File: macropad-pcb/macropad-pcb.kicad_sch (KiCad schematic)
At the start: 34 parts, among them SW1 SW_Push, U1 ATmega32U4-A, Y1 16MHz

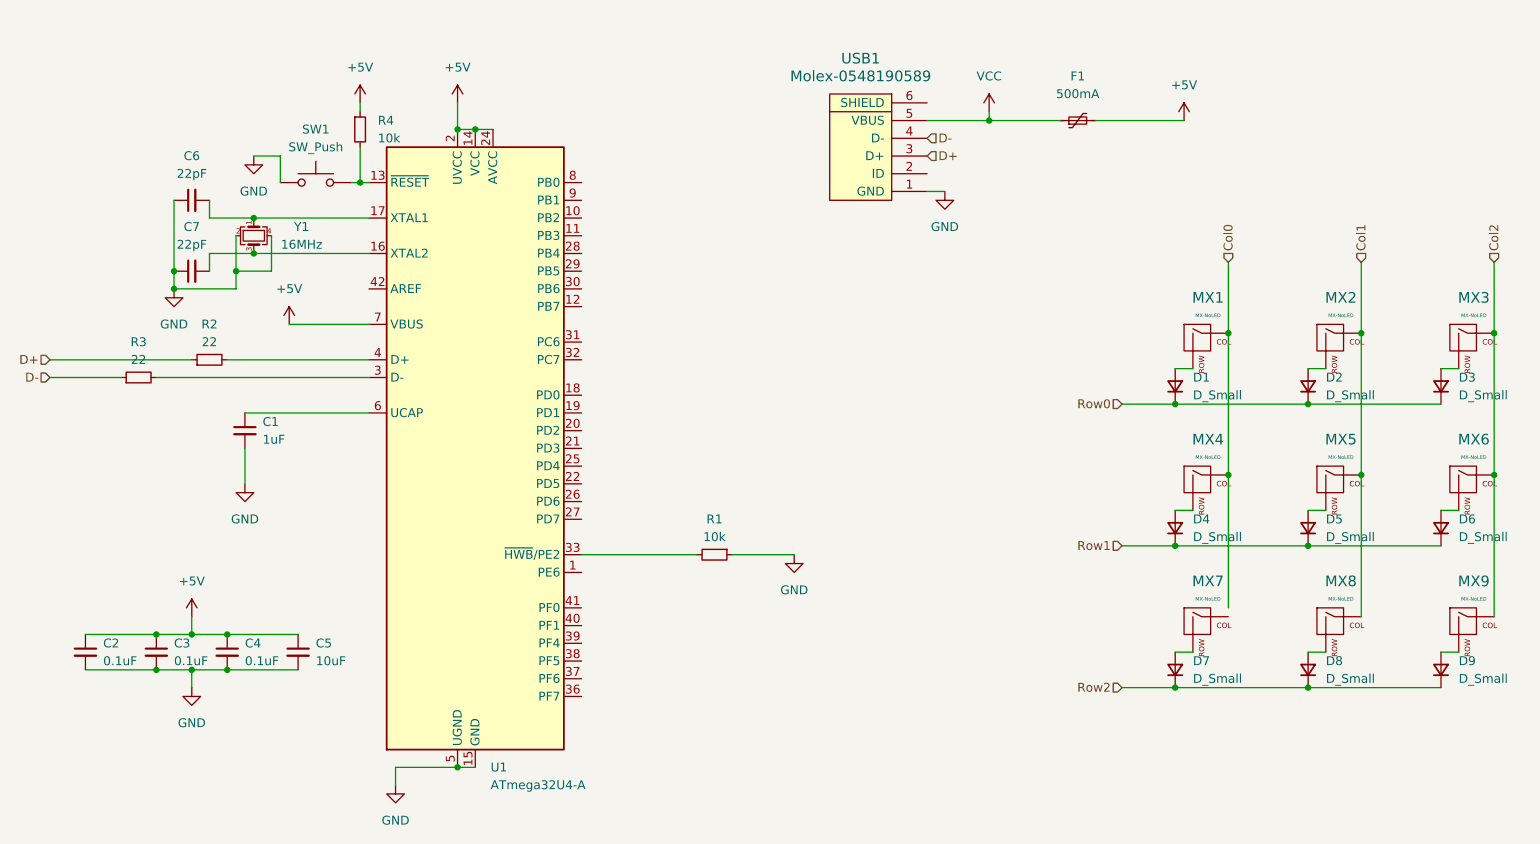
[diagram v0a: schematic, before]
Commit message: removed libraries in favor of using libraries straight from kicad, removed tracking of backups folder in version control, created and routed pcb
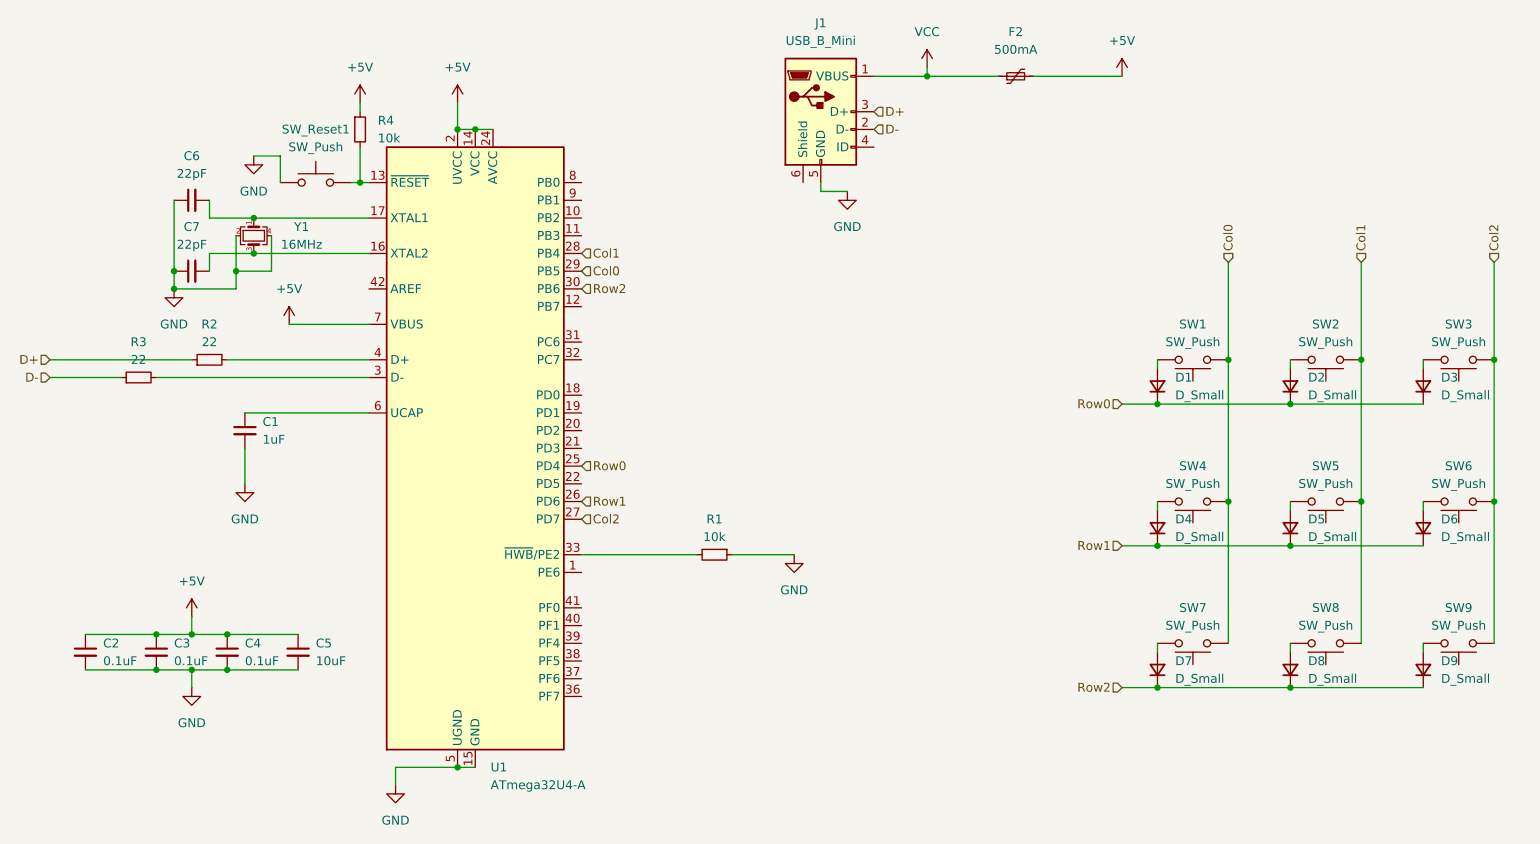
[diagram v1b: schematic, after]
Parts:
- removed F1: 500mA, Fuse:Fuse_1206_3216Metric, symbol Device:Polyfuse_Small
- removed MX1, MX2, MX3, MX4, MX5, MX6, MX7, MX8, MX9: MX-NoLED, MX_Alps_Hybrid:MX-1U-NoLED, symbol MX_Alps_Hybrid:MX-NoLED
- removed USB1: Molex-0548190589, random-keyboard-parts:Molex-0548190589, symbol random-keyboard-parts:Molex-0548190589
- added F2: 500mA, Fuse:Fuse_1206_3216Metric, symbol Device:Polyfuse_Small
- added J1: USB_B_Mini, Connector_USB:USB_Mini-B_Lumberg_2486_01_Horizontal, symbol Connector:USB_B_Mini
- added SW1, SW2, SW3, SW4, SW5, SW6, SW7, SW8, SW9: SW_Push, PCM_Switch_Keyboard_Hybrid:SW_Hybrid_Cherry_MX_Alps_1.00u, symbol Switch:SW_Push
- SW_Reset1: renamed from SW1; footprint random-keyboard-parts:SKQG-1155865 -> Button_Switch_SMD:SW_Push_1P1T_NO_CK_KMR2
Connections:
- net +5V: now also F2.2
- net Col0: now also U1.29 (PB5), SW1.1, SW4.1, SW7.1
- net Col1: now also U1.28 (PB4), SW2.1, SW5.1, SW8.1
- net Col2: now also U1.27 (PD7), SW3.1, SW6.1, SW9.1
- net D+: now also J1.3 (D+)
- net D-: now also J1.2 (D-)
- net GND: now also J1.5 (GND)
- net Row0: now also U1.25 (PD4)
- net Row1: now also U1.26 (PD6)
- net Row2: now also U1.30 (PB6)
- net VCC: now also F2.1, J1.1 (VBUS)
- net at D1.2 (A): now also SW1.2
- net at D4.2 (A): now also SW4.2
- net at D6.2 (A): now also SW6.2
- net at D7.2 (A): now also SW7.2
- net at D5.2 (A): now also SW5.2
- net at D9.2 (A): now also SW9.2
- net at D2.2 (A): now also SW2.2
- net at D8.2 (A): now also SW8.2
- net at D3.2 (A): now also SW3.2
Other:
- moved on the sheet: D1, D2, D3, D4, D5, D6, D7, D8, D9

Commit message: changed to just mx footprint since i haven't figured out how to handle the annular width issue of the hybrid footprint and made output files
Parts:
- SW1, SW2, SW3, SW4, SW5, SW6, SW7, SW8, SW9: footprint PCM_Switch_Keyboard_Hybrid:SW_Hybrid_Cherry_MX_Alps_1.00u -> PCM_Switch_Keyboard_Hotswap_Kailh:SW_Hotswap_Kailh_MX_Plated_1.00u
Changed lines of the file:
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@@
 			)
 		)
-		(property "Footprint" "PCM_Switch_Keyboard_Hybrid:SW_Hybrid_Cherry_MX_Alps_1.00u"
+		(property "Footprint" "PCM_Switch_Keyboard_Hotswap_Kailh:SW_Hotswap_Kailh_MX_Plated_1.00u"
 			(at 229.87 99.06 0)
 			(effects
@@
 			)
 		)
-		(property "Footprint" "PCM_Switch_Keyboard_Hybrid:SW_Hybrid_Cherry_MX_Alps_1.00u"
+		(property "Footprint" "PCM_Switch_Keyboard_Hotswap_Kailh:SW_Hotswap_Kailh_MX_Plated_1.00u"
 			(at 210.82 99.06 0)
 			(effects
@@
 			)
 		)
-		(property "Footprint" "PCM_Switch_Keyboard_Hybrid:SW_Hybrid_Cherry_MX_Alps_1.00u"
+		(property "Footprint" "PCM_Switch_Keyboard_Hotswap_Kailh:SW_Hotswap_Kailh_MX_Plated_1.00u"
 			(at 210.82 119.38 0)
 			(effects
@@
 			)
 		)
-		(property "Footprint" "PCM_Switch_Keyboard_Hybrid:SW_Hybrid_Cherry_MX_Alps_1.00u"
+		(property "Footprint" "PCM_Switch_Keyboard_Hotswap_Kailh:SW_Hotswap_Kailh_MX_Plated_1.00u"
 			(at 191.77 99.06 0)
 			(effects
@@
 			)
 		)
-		(property "Footprint" "PCM_Switch_Keyboard_Hybrid:SW_Hybrid_Cherry_MX_Alps_1.00u"
+		(property "Footprint" "PCM_Switch_Keyboard_Hotswap_Kailh:SW_Hotswap_Kailh_MX_Plated_1.00u"
 			(at 191.77 119.38 0)
 			(effects
@@
 			)
 		)
-		(property "Footprint" "PCM_Switch_Keyboard_Hybrid:SW_Hybrid_Cherry_MX_Alps_1.00u"
+		(property "Footprint" "PCM_Switch_Keyboard_Hotswap_Kailh:SW_Hotswap_Kailh_MX_Plated_1.00u"
 			(at 229.87 119.38 0)
 			(effects
@@
 			)
 		)
-		(property "Footprint" "PCM_Switch_Keyboard_Hybrid:SW_Hybrid_Cherry_MX_Alps_1.00u"
+		(property "Footprint" "PCM_Switch_Keyboard_Hotswap_Kailh:SW_Hotswap_Kailh_MX_Plated_1.00u"
 			(at 191.77 78.74 0)
 			(effects
@@
 			)
 		)
-		(property "Footprint" "PCM_Switch_Keyboard_Hybrid:SW_Hybrid_Cherry_MX_Alps_1.00u"
+		(property "Footprint" "PCM_Switch_Keyboard_Hotswap_Kailh:SW_Hotswap_Kailh_MX_Plated_1.00u"
 			(at 210.82 78.74 0)
 			(effects
@@
 			)
 		)
-		(property "Footprint" "PCM_Switch_Keyboard_Hybrid:SW_Hybrid_Cherry_MX_Alps_1.00u"
+		(property "Footprint" "PCM_Switch_Keyboard_Hotswap_Kailh:SW_Hotswap_Kailh_MX_Plated_1.00u"
 			(at 229.87 78.74 0)
 			(effects
